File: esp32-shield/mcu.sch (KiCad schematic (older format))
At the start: 25 parts, among them J11 DNP, J5 Conn_01x14_Female, J6 Conn_01x14_Female, Q3 S8050, Q4 S8050, SW1 DNP, U13 ESP32-WROOM32, U14 W25Q32JVSS, U5 CH340G, U6 AMS1117-3.3, Y1 12MHZ

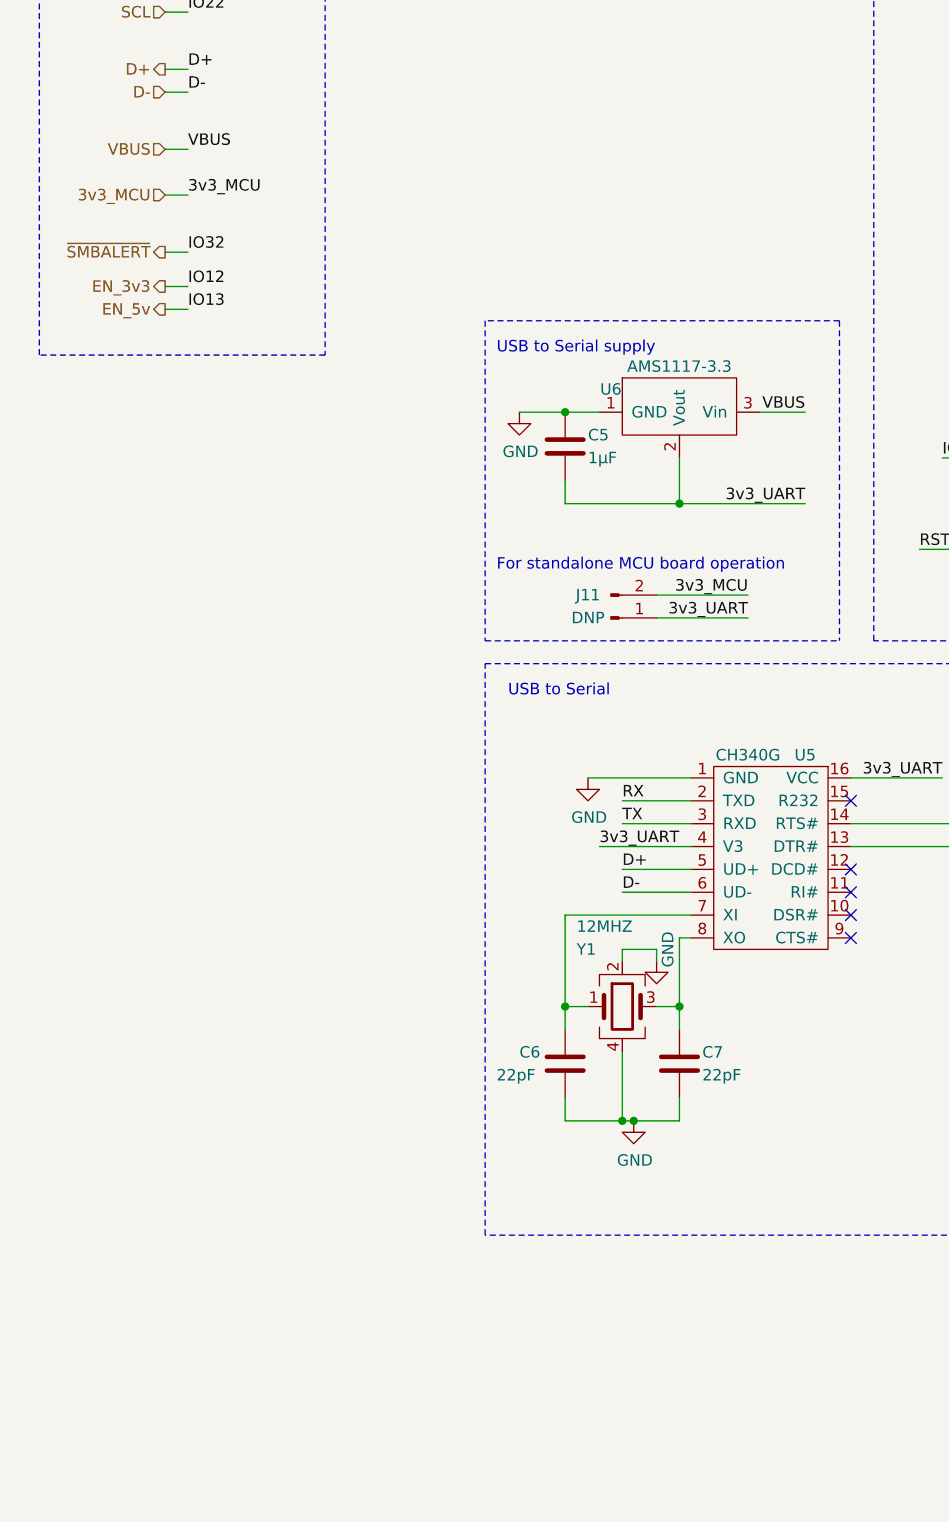
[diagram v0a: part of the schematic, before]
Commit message: added rgbw led, swapped ch340g for ch340c part numers
also marked crystal and caps as DNP
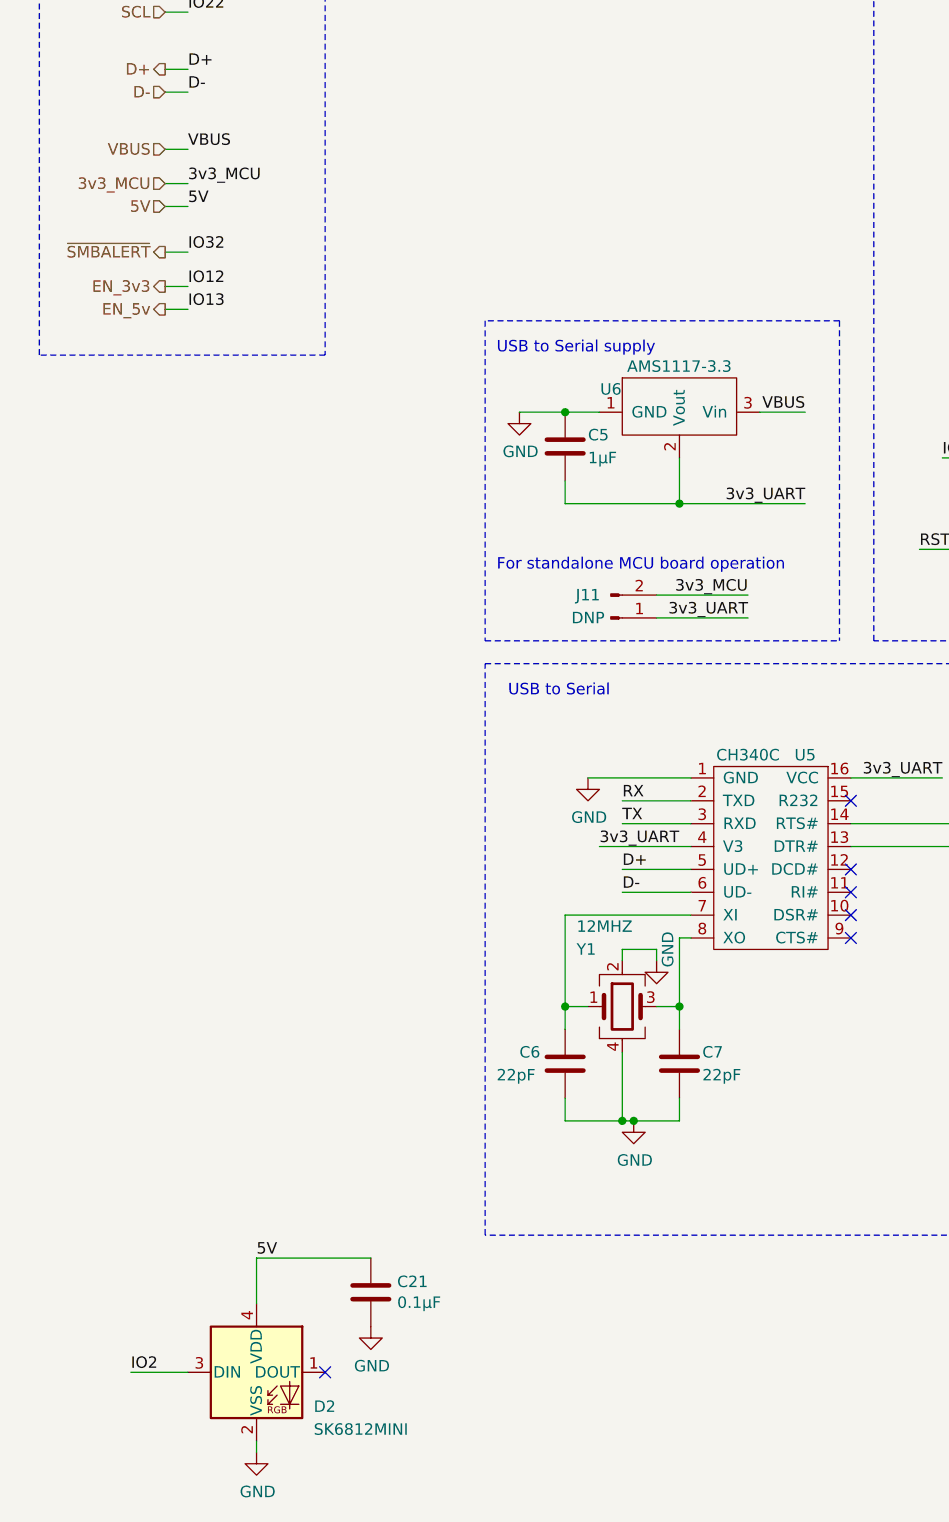
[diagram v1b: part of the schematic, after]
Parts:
- added C21: 0.1µF, Capacitor_SMD:C_0603_1608Metric_Pad1.05x0.95mm_HandSolder, symbol Device:C
- added D2: SK6812MINI, LED_SMD:LED_SK6812MINI_PLCC4_3.5x3.5mm_P1.75mm, symbol LED:SK6812MINI
- C6, C7, Y1: DNP (none) -> DNP
- U5: value CH340G -> CH340C; LCSC C14267 -> C84681
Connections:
- net GND: now also C21.2, D2.2 (VSS)
- net IO2: now also D2.3 (DIN)
- new net 5V: C21.1, D2.4 (VDD)
- no-connect marks 8 -> 9
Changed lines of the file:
@@
 $Descr A4 11693 8268
 encoding utf-8
-Sheet 5 2
+Sheet 2 2
 Title "SuperPower-uC"
 Date "2020-09-20"
@@
 NoConn ~ 6900 3200
 NoConn ~ 6800 3200
-Wire Wire Line
-	7300 3450 7300 3200
 Wire Wire Line
 	7200 3450 7200 3200
@@
 Text Label 7200 3450 1    50   ~ 0
 IO15
-Text Label 7300 3450 1    50   ~ 0
-IO2
 $Comp
 L power:GND #PWR0118
@@
 Text Label 9700 2350 0    50   ~ 0
 IO15
-Text HLabel 1150 1900 0    50   Input ~ 0
+Text HLabel 1150 1850 0    50   Input ~ 0
 3v3_MCU
 $Comp
@@
 	4800 1650 5200 1650
 Wire Wire Line
-	1150 1900 1250 1900
+	1150 1850 1250 1850
 Text Label 4800 1950 0    50   ~ 0
 RST
-Text Label 1250 1900 0    50   ~ 0
+Text Label 1250 1850 0    50   ~ 0
 3v3_MCU
 Wire Notes Line
@@
 F 3 "~" H 3400 5700 50  0001 C CNN
 F 4 "C1653" H 3400 5700 50  0001 C CNN "LCSC"
+F 5 "DNP" H 3400 5700 50  0001 C CNN "DNP"
 	1    3400 5700
 	1    0    0    -1
@@
 F 3 "~" H 2900 5700 50  0001 C CNN
 F 4 "C1653" H 2900 5700 50  0001 C CNN "LCSC"
+F 5 "DNP" H 2900 5700 50  0001 C CNN "DNP"
 	1    2900 5700
 	1    0    0    -1
@@
 AR Path="/5F63A193/5FEC8BEB" Ref="U5"  Part="1"
 F 0 "U5" H 3950 4750 50  0000 C CNN
-F 1 "CH340G" H 3700 4750 50  0000 C CNN
+F 1 "CH340C" H 3700 4750 50  0000 C CNN
 F 2 "Package_SO:SOP-16_4.55x10.3mm_P1.27mm" H 4000 4750 50  0001 C CNN
 F 3 "https://www.mpja.com/download/35227cpdata.pdf" H 4000 4750 50  0001 C CNN
-F 4 "C14267" H 3800 4550 50  0001 C CNN "LCSC"
+F 4 "C84681" H 3800 4550 50  0001 C CNN "LCSC"
 	1    3800 4550
 	1    0    0    -1
@@
 F 3 "https://datasheet.lcsc.com/szlcsc/Yangxing-Tech-X322512MSB4SI_C9002.pdf" H 3150 5450 50  0001 C CNN
 F 4 "C9002" H 3150 5450 50  0001 C CNN "LCSC"
+F 5 "DNP" H 3150 5450 50  0001 C CNN "DNP"
 	1    3150 5450
 	1    0    0    -1
@@
 Text Label 4550 3050 0    50   ~ 0
 IO2
+$Comp
+L LED:SK6812MINI D2
+U 1 1 60359CD9
+P 1550 7050
+F 0 "D2" H 1800 6900 50  0000 L CNN
+F 1 "SK6812MINI" H 1800 6800 50  0000 L CNN
+F 2 "LED_SMD:LED_SK6812MINI_PLCC4_3.5x3.5mm_P1.75mm" H 1600 6750 50  0001 L TNN
+F 3 "https://cdn-shop.adafruit.com/product-files/2686/SK6812MINI_REV.01-1-2.pdf" H 1650 6675 50  0001 L TNN
+	1    1550 7050
+	1    0    0    -1
+$EndComp
+Text HLabel 1150 1950 0    50   Input ~ 0
+5V
+Wire Wire Line
+	1150 1950 1250 1950
+Text Label 1250 1950 0    50   ~ 0
+5V
+Text Label 1550 6550 0    50   ~ 0
+5V
+$Comp
+L Device:C C21
+U 1 1 603835DD
+P 2050 6700
+F 0 "C21" H 2165 6746 50  0000 L CNN
+F 1 "0.1µF" H 2165 6655 50  0000 L CNN
+F 2 "Capacitor_SMD:C_0603_1608Metric_Pad1.05x0.95mm_HandSolder" H 2088 6550 50  0001 C CNN
+F 3 "~" H 2050 6700 50  0001 C CNN
+F 4 "C14858" H 2050 6700 50  0001 C CNN "LCSC"
+	1    2050 6700
+	1    0    0    -1
+$EndComp
+$Comp
+L power:GND #PWR?
+U 1 1 603847FA
+P 1550 7400
+AR Path="/5F63B107/603847FA" Ref="#PWR?"  Part="1"
+AR Path="/5F63A193/603847FA" Ref="#PWR0101"  Part="1"
+F 0 "#PWR0101" H 1550 7150 50  0001 C CNN
+F 1 "GND" H 1555 7227 50  0000 C CNN
+F 2 "" H 1550 7400 50  0001 C CNN
+F 3 "" H 1550 7400 50  0001 C CNN
+	1    1550 7400
+	1    0    0    -1
+$EndComp
+$Comp
+L power:GND #PWR?
+U 1 1 60385656
+P 2050 6850
+AR Path="/5F63B107/60385656" Ref="#PWR?"  Part="1"
+AR Path="/5F63A193/60385656" Ref="#PWR0102"  Part="1"
+F 0 "#PWR0102" H 2050 6600 50  0001 C CNN
+F 1 "GND" H 2055 6677 50  0000 C CNN
+F 2 "" H 2050 6850 50  0001 C CNN
+F 3 "" H 2050 6850 50  0001 C CNN
+	1    2050 6850
+	1    0    0    -1
+$EndComp
+Wire Wire Line
+	2050 6550 1550 6550
+Wire Wire Line
+	1550 6550 1550 6750
+Wire Wire Line
+	1250 7050 1000 7050
+NoConn ~ 1850 7050
+Text Label 7300 3450 1    50   ~ 0
+IO2
+Wire Wire Line
+	7300 3450 7300 3200
+Text Label 1000 7050 0    50   ~ 0
+IO2
+Wire Wire Line
+	1550 7350 1550 7400
 $EndSCHEMATC
